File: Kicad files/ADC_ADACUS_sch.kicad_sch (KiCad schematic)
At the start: 32 parts, among them U301 REF3033, U302 MCP6001UT-E/OT, U303 MCP6001UT-E/OT

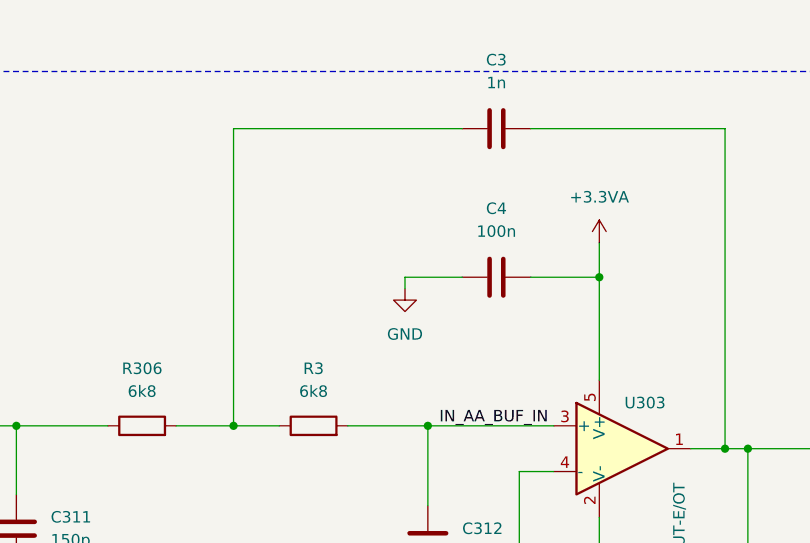
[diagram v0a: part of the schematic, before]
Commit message: [FILE] Finished board
Added PCB documents and finished schematics. Project is now done with both Altium and Kicad files uploaded
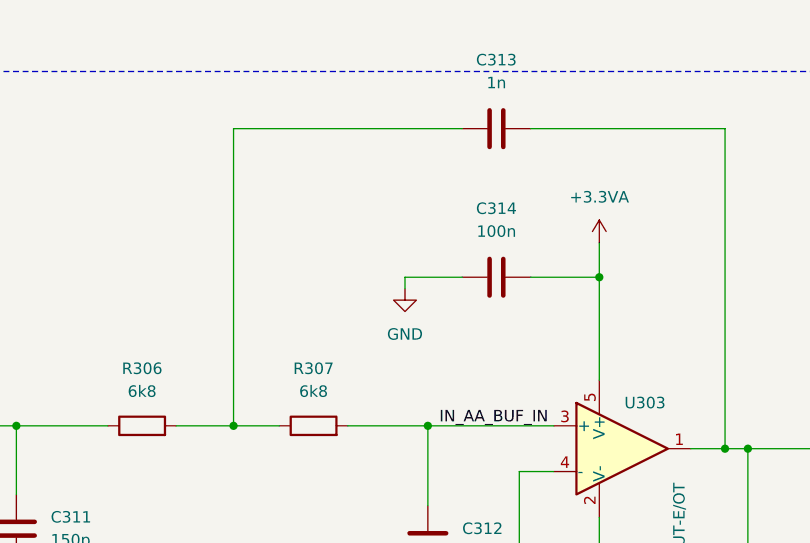
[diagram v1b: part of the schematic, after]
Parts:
- C300, C301, C302, C304, C307: footprint (none) -> Capacitor_SMD:C_0603_1608Metric
- C303, C305, C306, C308, C309, C310, C311, C312, C315: footprint (none) -> Capacitor_SMD:C_0402_1005Metric
- C313: renamed from C3; footprint (none) -> Capacitor_SMD:C_0402_1005Metric
- C314: renamed from C4; footprint (none) -> Capacitor_SMD:C_0402_1005Metric
- D300: value PESD3V3L1UB,115 -> PESD3V3L1UB,115; footprint (none) -> Diode_SMD:D_SOD-523
- J300: footprint (none) -> Connector_Coaxial:BNC_Amphenol_B6252HB-NPP3G-50_Horizontal
- R300, R301, R302, R303, R304, R305, R306, R308, R309: footprint (none) -> Resistor_SMD:R_0402_1005Metric
- R307: renamed from R3; footprint (none) -> Resistor_SMD:R_0402_1005Metric
- U300: footprint (none) -> Package_SO:VSSOP-10_3x3mm_P0.5mm
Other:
- company: (none) -> Head-Pin (TS)
- title: (none) -> ADC Schematic
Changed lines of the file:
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@@
 	(generator_version "8.0")
 	(paper "A4")
+	(title_block
+		(title "ADC Schematic")
+		(date "2024-08-06")
+		(company "Head-Pin (TS)")
+	)
 	(junction
 		(at 59.69 88.9)
@@
 		(dnp no)
 		(fields_autoplaced yes)
-		(property "Reference" "C4"
+		(property "Reference" "C314"
 			(at 210.82 46.99 90)
 			(effects
@@
 			)
 		)
-		(property "Footprint" ""
+		(property "Footprint" "Capacitor_SMD:C_0402_1005Metric"
 			(at 214.63 53.6448 0)
 			(effects
@@
 			(project "ADACUS"
 				(path "/5b4caae3-37f5-49e8-8ccb-da7cc544f604/3a988b36-57d2-4e88-bd76-42555a652ede"
-					(reference "C4")
+					(reference "C314")
 					(unit 1)
 				)
@@
 			)
 		)
-		(property "Footprint" ""
+		(property "Footprint" "Resistor_SMD:R_0402_1005Metric"
 			(at 45.72 70.358 90)
 			(effects
@@
 			)
 		)
-		(property "Footprint" ""
+		(property "Footprint" "Package_SO:VSSOP-10_3x3mm_P0.5mm"
 			(at 124.46 161.29 0)
 			(effects
@@
 			)
 		)
-		(property "Footprint" ""
+		(property "Footprint" "Capacitor_SMD:C_0402_1005Metric"
 			(at 141.9352 138.43 0)
 			(effects
@@
 			)
 		)
-		(property "Footprint" ""
+		(property "Footprint" "Resistor_SMD:R_0402_1005Metric"
 			(at 27.94 160.528 90)
 			(effects
@@
 			)
 		)
-		(property "Value" "PESD3V3L1UB,115 "
+		(property "Value" "PESD3V3L1UB,115"
 			(at 38.1 81.28 90)
 			(effects
@@
 			)
 		)
-		(property "Footprint" ""
+		(property "Footprint" "Diode_SMD:D_SOD-523"
 			(at 34.29 78.74 0)
 			(effects
@@
 			)
 		)
-		(property "Footprint" ""
+		(property "Footprint" "Capacitor_SMD:C_0603_1608Metric"
 			(at 18.7452 170.18 0)
 			(effects
@@
 			)
 		)
-		(property "Footprint" ""
+		(property "Footprint" "Resistor_SMD:R_0402_1005Metric"
 			(at 149.86 163.068 90)
 			(effects
@@
 			)
 		)
-		(property "Footprint" ""
+		(property "Footprint" "Capacitor_SMD:C_0402_1005Metric"
 			(at 87.63 67.6148 0)
 			(effects
@@
 			)
 		)
-		(property "Footprint" ""
+		(property "Footprint" "Capacitor_SMD:C_0402_1005Metric"
 			(at 267.6652 88.9 0)
 			(effects
@@
 			)
 		)
-		(property "Footprint" ""
+		(property "Footprint" "Capacitor_SMD:C_0603_1608Metric"
 			(at 40.3352 170.18 0)
 			(effects
@@
 			)
 		)
-		(property "Footprint" ""
+		(property "Footprint" "Resistor_SMD:R_0402_1005Metric"
 			(at 257.81 75.438 90)
 			(effects
@@
 			)
 		)
-		(property "Footprint" ""
+		(property "Footprint" "Capacitor_SMD:C_0603_1608Metric"
 			(at 154.6352 138.43 0)
 			(effects
@@
 			)
 		)
-		(property "Footprint" ""
+		(property "Footprint" "Resistor_SMD:R_0402_1005Metric"
 			(at 99.568 58.42 90)
 			(effects
@@
 			)
 		)
-		(property "Footprint" ""
+		(property "Footprint" "Capacitor_SMD:C_0603_1608Metric"
 			(at 98.7552 138.43 0)
 			(effects
@@
 		(dnp no)
 		(fields_autoplaced yes)
-		(property "Reference" "C3"
+		(property "Reference" "C313"
 			(at 210.82 30.48 90)
 			(effects
@@
 			)
 		)
-		(property "Footprint" ""
+		(property "Footprint" "Capacitor_SMD:C_0402_1005Metric"
 			(at 214.63 37.1348 0)
 			(effects
@@
 			(project "ADACUS"
 				(path "/5b4caae3-37f5-49e8-8ccb-da7cc544f604/3a988b36-57d2-4e88-bd76-42555a652ede"
-					(reference "C3")
+					(reference "C313")
 					(unit 1)
 				)
@@
 			)
 		)
-		(property "Footprint" ""
+		(property "Footprint" "Resistor_SMD:R_0402_1005Metric"
 			(at 257.81 97.028 90)
 			(effects
@@
 			)
 		)
-		(property "Footprint" ""
+		(property "Footprint" "Capacitor_SMD:C_0402_1005Metric"
 			(at 73.3552 82.55 0)
 			(effects
@@
 			)
 		)
-		(property "Footprint" ""
+		(property "Footprint" "Connector_Coaxial:BNC_Amphenol_B6252HB-NPP3G-50_Horizontal"
 			(at 21.59 68.58 0)
 			(effects
@@
 		(dnp no)
 		(fields_autoplaced yes)
-		(property "Reference" "R3"
+		(property "Reference" "R307"
 			(at 190.5 64.77 90)
 			(effects
@@
 			)
 		)
-		(property "Footprint" ""
+		(property "Footprint" "Resistor_SMD:R_0402_1005Metric"
 			(at 190.5 72.898 90)
 			(effects
@@
 			(project "ADACUS"
 				(path "/5b4caae3-37f5-49e8-8ccb-da7cc544f604/3a988b36-57d2-4e88-bd76-42555a652ede"
-					(reference "R3")
+					(reference "R307")
 					(unit 1)
 				)
@@
 			)
 		)
-		(property "Footprint" ""
+		(property "Footprint" "Capacitor_SMD:C_0402_1005Metric"
 			(at 98.7552 176.53 0)
 			(effects
@@
 			)
 		)
-		(property "Footprint" ""
+		(property "Footprint" "Capacitor_SMD:C_0402_1005Metric"
 			(at 112.7252 138.43 0)
 			(effects
@@
 			)
 		)
-		(property "Footprint" ""
+		(property "Footprint" "Resistor_SMD:R_0402_1005Metric"
 			(at 171.45 72.898 90)
 			(effects
@@
 			)
 		)
-		(property "Footprint" ""
+		(property "Footprint" "Capacitor_SMD:C_0603_1608Metric"
 			(at 86.0552 176.53 0)
 			(effects
@@
 			)
 		)
-		(property "Footprint" ""
+		(property "Footprint" "Capacitor_SMD:C_0402_1005Metric"
 			(at 118.11 54.9148 0)
 			(effects
@@
 			)
 		)
-		(property "Footprint" ""
+		(property "Footprint" "Resistor_SMD:R_0402_1005Metric"
 			(at 61.468 78.74 90)
 			(effects
@@
 			)
 		)
-		(property "Footprint" ""
+		(property "Footprint" "Capacitor_SMD:C_0402_1005Metric"
 			(at 204.1652 87.63 0)
 			(effects
@@
 			)
 		)
-		(property "Footprint" ""
+		(property "Footprint" "Resistor_SMD:R_0402_1005Metric"
 			(at 142.24 72.898 90)
 			(effects
@@
 			)
 		)
-		(property "Footprint" ""
+		(property "Footprint" "Capacitor_SMD:C_0402_1005Metric"
 			(at 158.4452 86.36 0)
 			(effects
